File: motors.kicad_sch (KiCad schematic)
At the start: 76 parts, among them CN101 Conn_01x04_Socket, IC102 CXA1082BQ, IC103 RC4558, IC104 BA6290A, IC105 BA6290A, P104 Conn_01x06_Pin, P106 Conn_01x02_Pin, Q102 DTC114EU3, Q103 2SC2412K

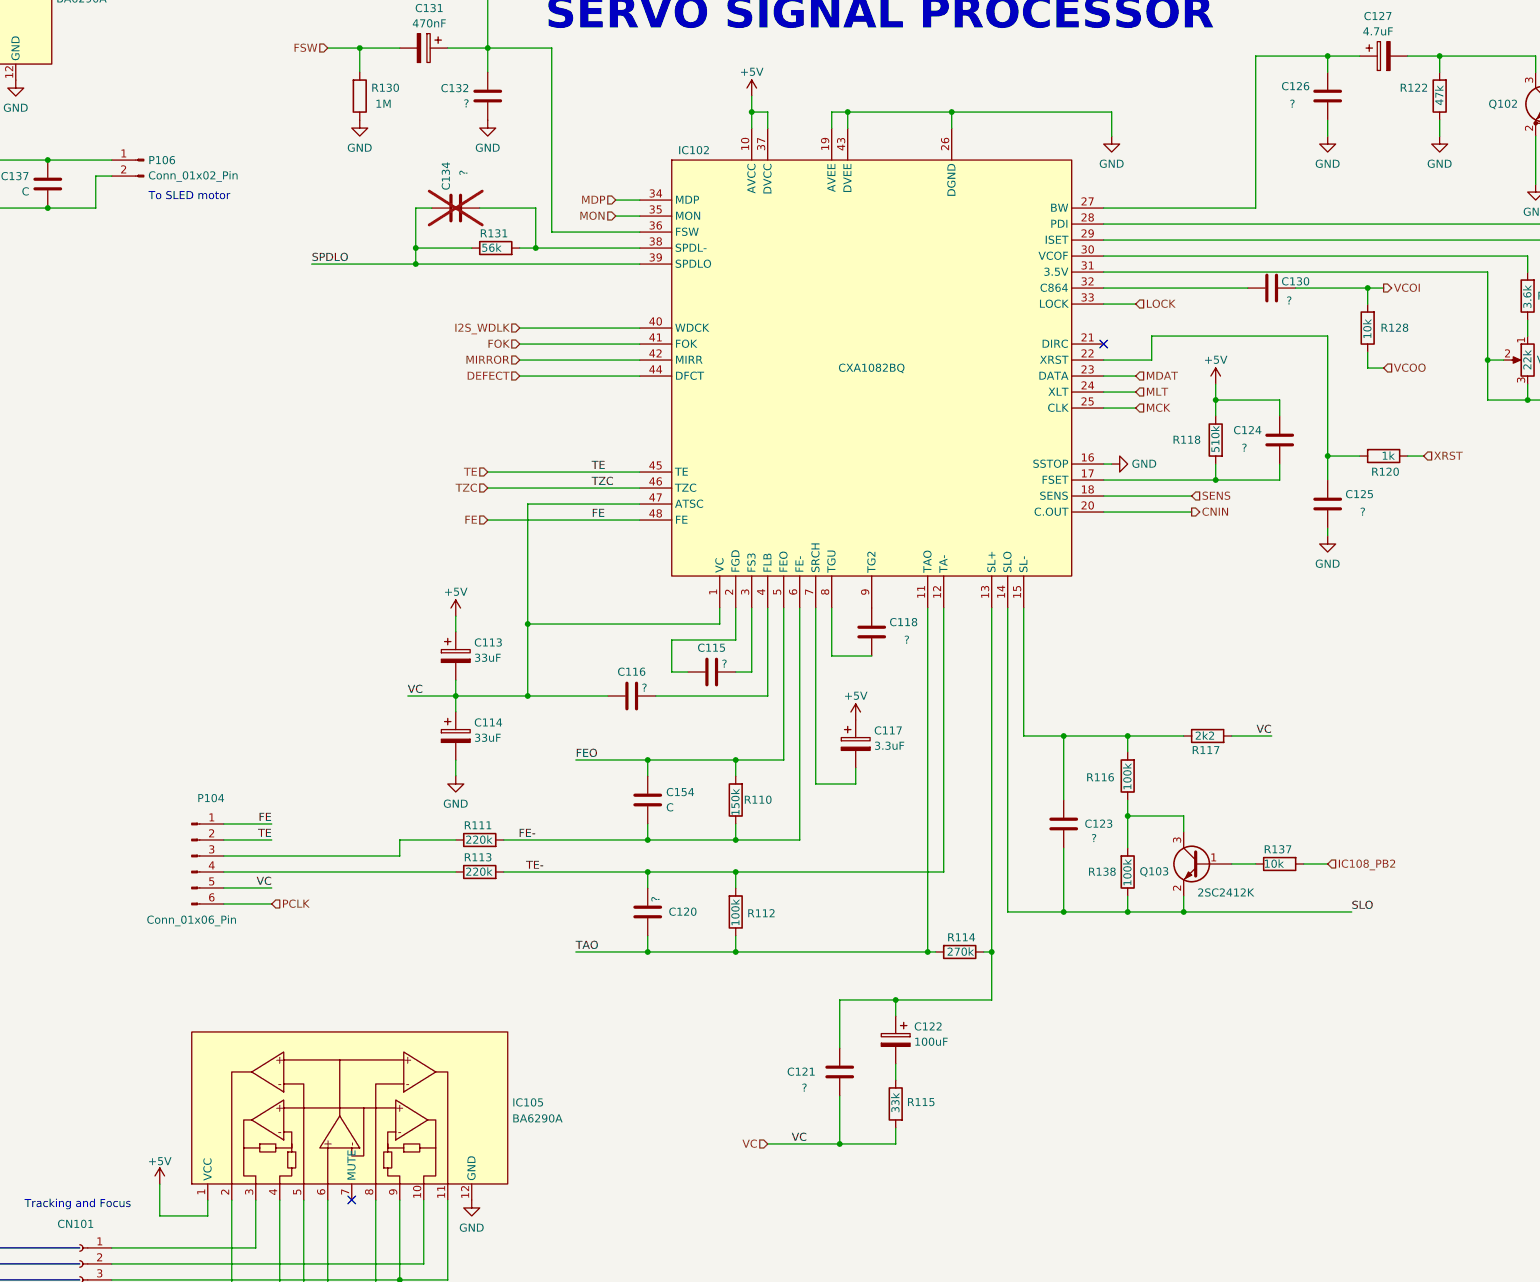
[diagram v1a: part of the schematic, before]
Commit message: Small update, some typo fixes, more comments added to help understanding
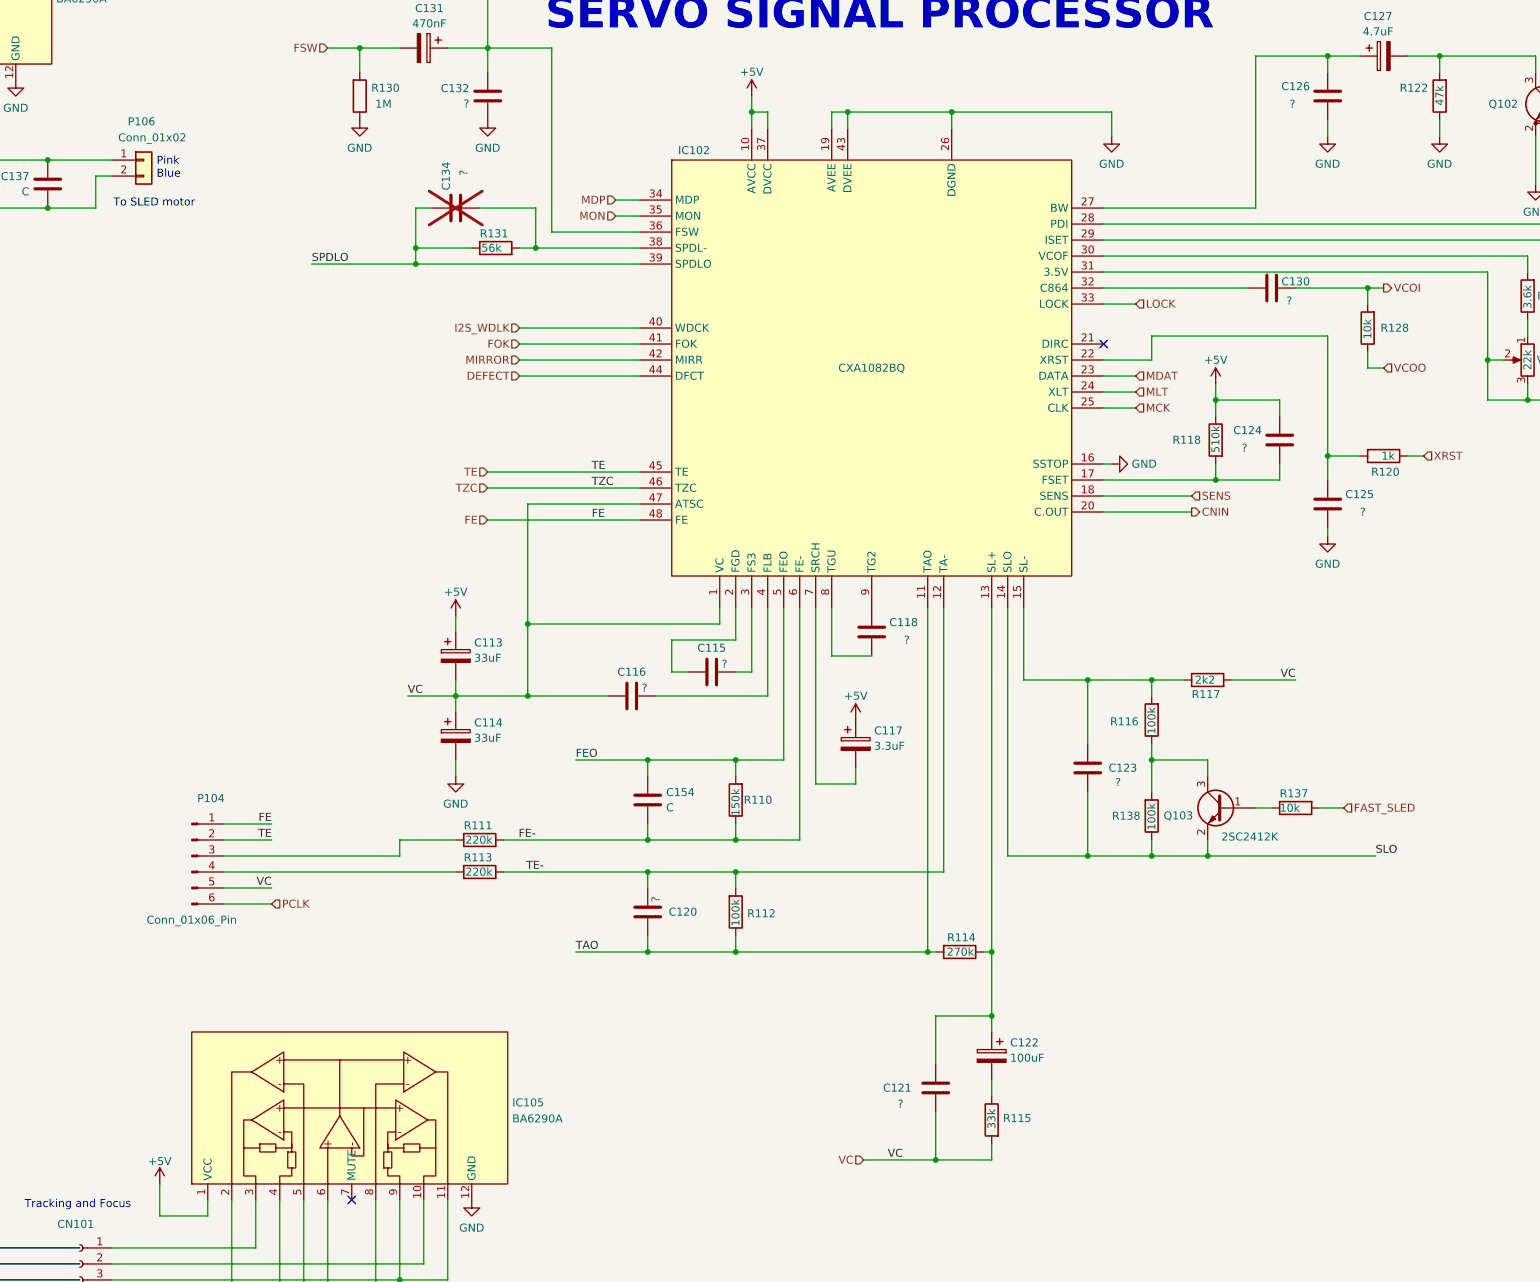
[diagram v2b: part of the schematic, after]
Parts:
- removed P106: Conn_01x02_Pin, symbol Connector:Conn_01x02_Pin
- added P106: Conn_01x02, Connector_JST:JST_ZE_B02B-ZESK-1D_1x02_P1.50mm_Vertical, symbol Connector_Generic:Conn_01x02
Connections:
- net at C137.1, IC104.11, IC104.9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: now also P106.1 (Pin_1)
- net at C137.2, IC104.10: now also P106.2 (Pin_2)
- net IC108_PB2 renamed FAST_SLED
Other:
- note added: "Pink Blue"
- moved on the sheet: C121, C122, C123, Q103, R115, R116, R117, R137, R138

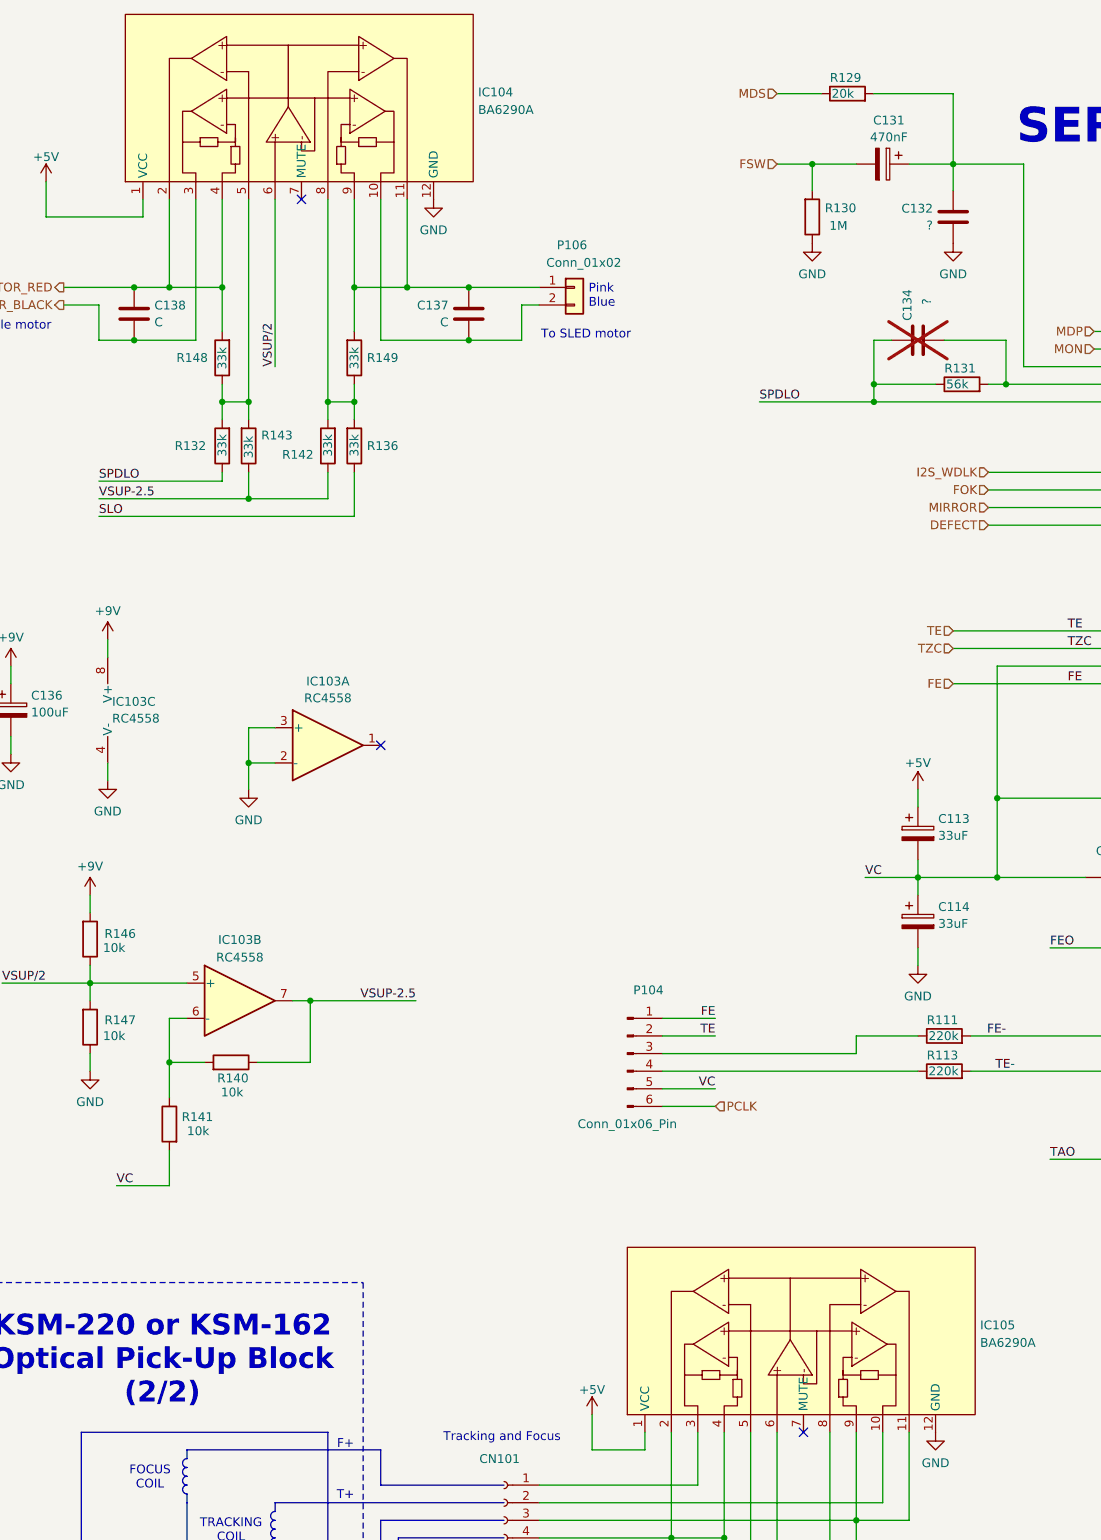
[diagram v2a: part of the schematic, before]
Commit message: KSS-220A Flexible PCBs ready and on order for trial.
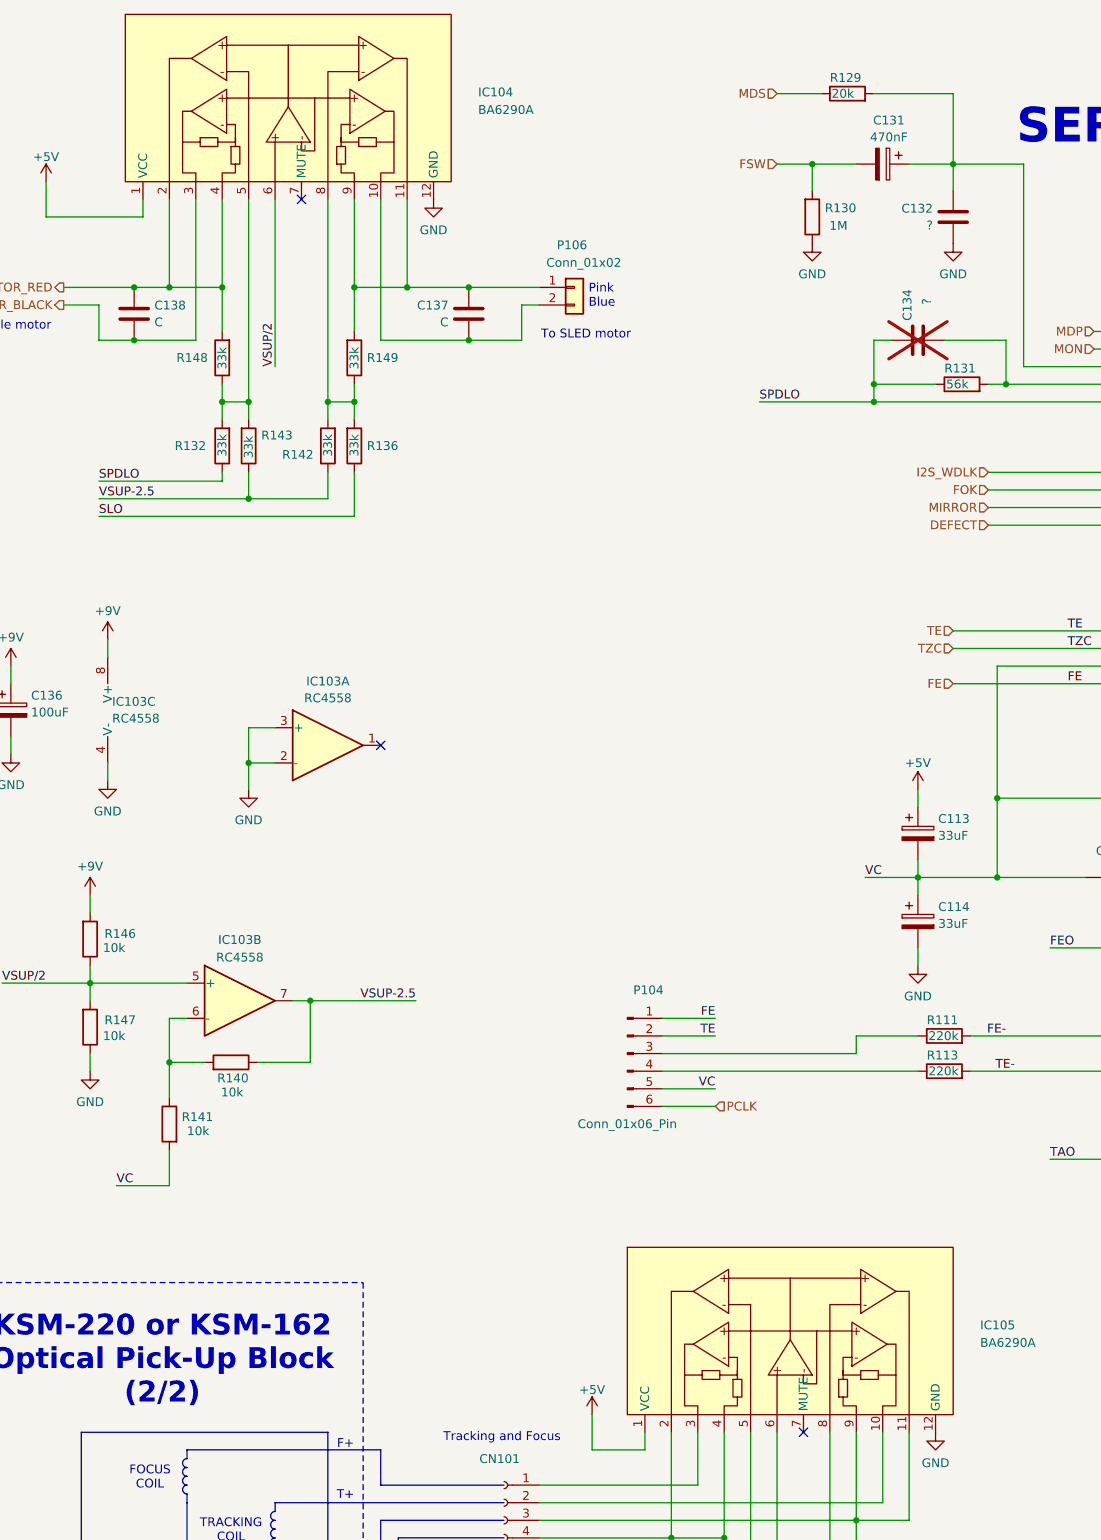
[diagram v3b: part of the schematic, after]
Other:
- moved on the sheet: IC104, IC105
